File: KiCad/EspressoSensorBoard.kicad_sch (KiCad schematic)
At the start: 15 parts, among them IC1 FDC1004DGSR, J1 GRAPHIC DISPLAY IPS - 1.69", J2 MAX31855 (Temperature), J3 Screw_Terminal_01x02, J5 Pressure_Sensor, J7 Arduino_Nano_v3_Left, J8 Arduino_Nano_v3_Right, J9 Water_Level_Electrodes

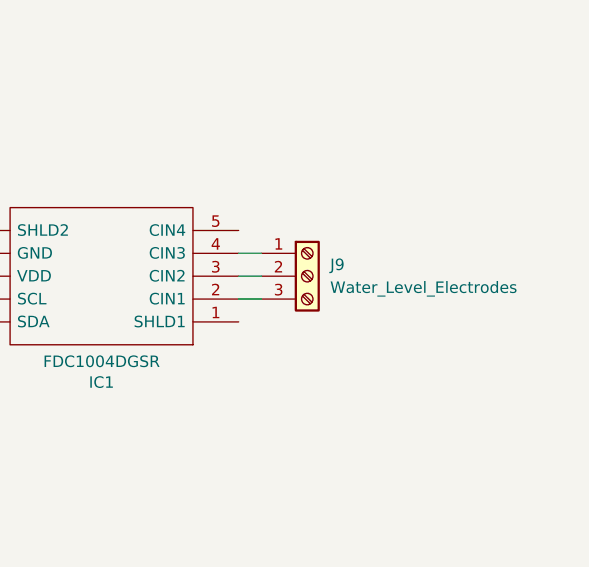
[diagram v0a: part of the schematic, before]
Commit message: Use SCHLD1 pin from the FDC1004 capacitive sensor
https://github.com/jcohenadad/espresso-pimpup/issues/43
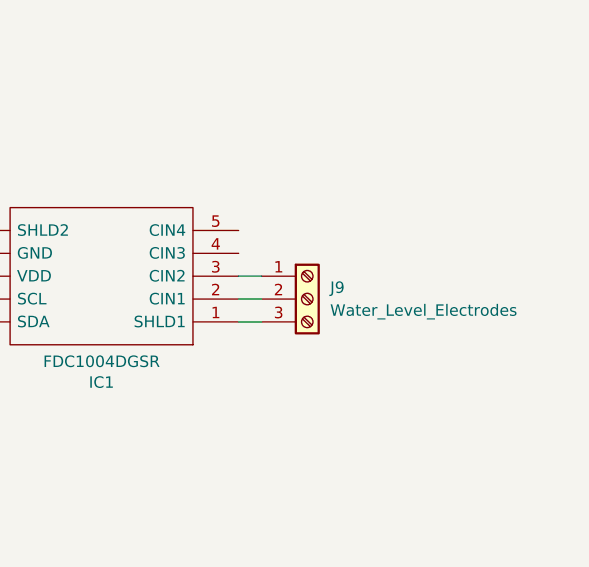
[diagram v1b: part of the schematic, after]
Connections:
- net at IC1.1 (SHLD1): now also J9.3 (Pin_3)
- net at IC1.2 (CIN1): now also J9.2 (Pin_2); no longer J9.3 (Pin_3)
- net at IC1.3 (CIN2): now also J9.1 (Pin_1); no longer J9.2 (Pin_2)
- net at IC1.4 (CIN3): no longer J9.1 (Pin_1)
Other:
- moved on the sheet: J9
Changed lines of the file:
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@@
+	(wire
+		(pts
+			(xy 222.25 58.42) (xy 224.79 58.42)
+		)
+		(stroke
+			(width 0)
+			(type default)
+		)
+	)
 	(wire
 		(pts
@@
 	(wire
 		(pts
-			(xy 222.25 58.42) (xy 224.79 58.42)
-		)
-		(stroke
-			(width 0)
-			(type default)
-		)
-	)
-	(wire
-		(pts
 			(xy 124.46 76.2) (xy 134.62 76.2)
 		)
@@
 	(wire
 		(pts
-			(xy 222.25 55.88) (xy 224.79 55.88)
-		)
-		(stroke
-			(width 0)
-			(type default)
-		)
-	)
-	(wire
-		(pts
 			(xy 130.81 63.5) (xy 134.62 63.5)
 		)
@@
 		(pts
 			(xy 222.25 60.96) (xy 224.79 60.96)
+		)
+		(stroke
+			(width 0)
+			(type default)
+		)
+	)
+	(wire
+		(pts
+			(xy 222.25 63.5) (xy 224.79 63.5)
 		)
 		(stroke
@@
 	(symbol
 		(lib_id "Connector:Screw_Terminal_01x03")
-		(at 229.87 58.42 0)
+		(at 229.87 60.96 0)
 		(unit 1)
 		(exclude_from_sim no)
@@
 		(fields_autoplaced yes)
 		(property "Reference" "J9"
-			(at 232.41 57.1499 0)
+			(at 232.41 59.6899 0)
 			(effects
 				(font
@@
 		)
 		(property "Value" "Water_Level_Electrodes"
-			(at 232.41 59.6899 0)
+			(at 232.41 62.2299 0)
 			(effects
 				(font
@@
 		)
 		(property "Footprint" "Connector_PinHeader_2.54mm:PinHeader_1x03_P2.54mm_Vertical"
-			(at 229.87 58.42 0)
+			(at 229.87 60.96 0)
 			(effects
 				(font
@@
 		)
 		(property "Datasheet" "~"
-			(at 229.87 58.42 0)
+			(at 229.87 60.96 0)
 			(effects
 				(font
@@
 		)
 		(property "Description" "Generic screw terminal, single row, 01x03, script generated (kicad-library-utils/schlib/autogen/connector/)"
-			(at 229.87 58.42 0)
-			(effects
-				(font
+			(at 229.87 60.96 0)
+			(effects
+				(font

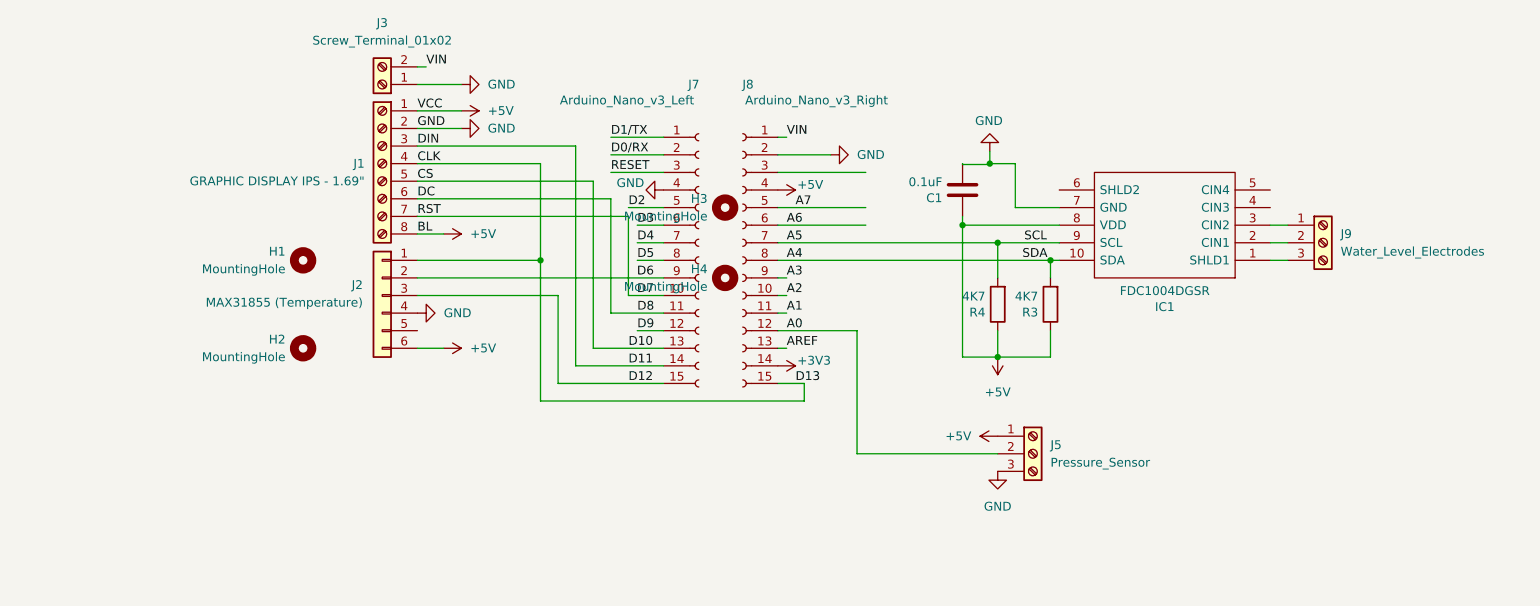
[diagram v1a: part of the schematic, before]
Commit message: Replaced screw terminal by Dupont male pins
https://github.com/jcohenadad/espresso-pimpup/issues/38
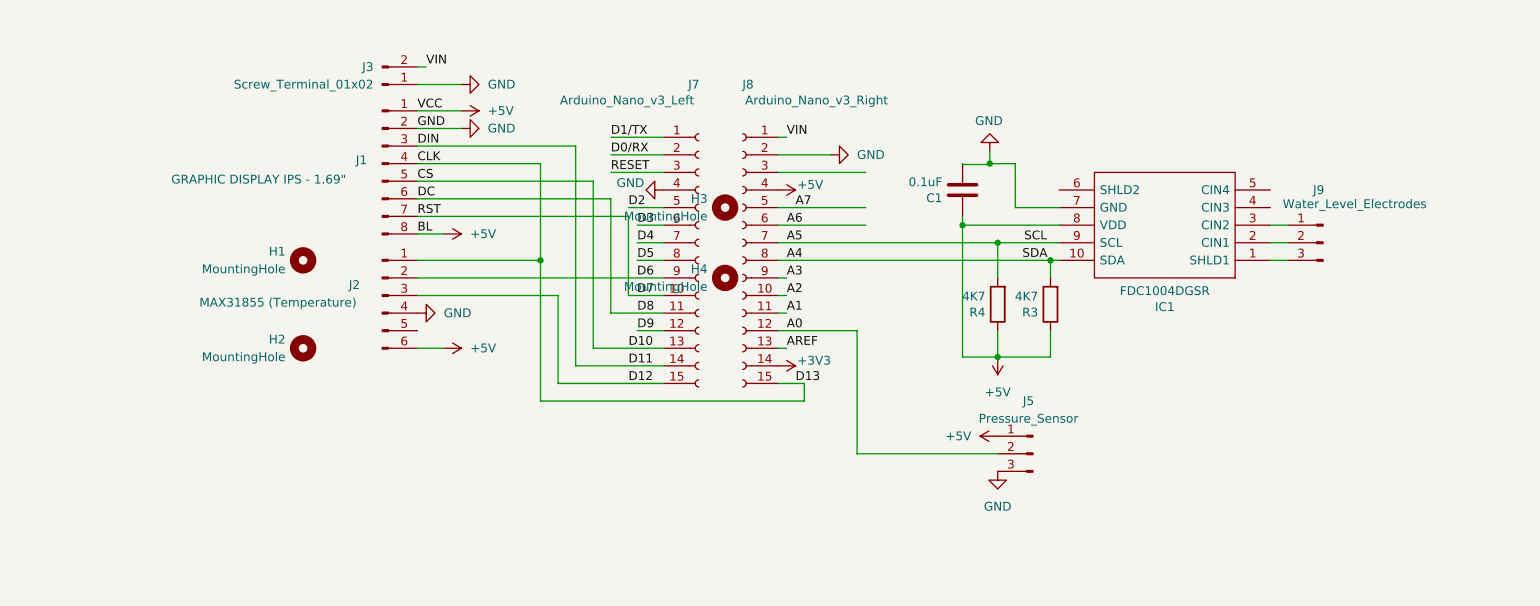
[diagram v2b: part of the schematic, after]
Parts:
- J1: symbol Connector:Screw_Terminal_01x08 -> Connector:Conn_01x08_Pin
- J2: symbol Connector_Generic:Conn_01x06 -> Connector:Conn_01x06_Pin
- J3: symbol Connector:Screw_Terminal_01x02 -> Connector:Conn_01x02_Pin
- J5, J9: symbol Connector:Screw_Terminal_01x03 -> Connector:Conn_01x03_Pin
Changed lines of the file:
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@@
 	)
 	(symbol
-		(lib_id "Connector_Generic:Conn_01x06")
+		(lib_id "Connector:Conn_01x06_Pin")
 		(at 93.98 68.58 0)
-		(mirror y)
 		(unit 1)
 		(exclude_from_sim no)
@@
 		(dnp no)
 		(property "Reference" "J2"
-			(at 91.186 67.056 0)
+			(at 89.154 67.056 0)
 			(effects
 				(font
@@
 		)
 		(property "Value" "MAX31855 (Temperature)"
-			(at 91.186 69.596 0)
+			(at 67.564 69.596 0)
 			(effects
 				(font
@@
 			)
 		)
-		(property "Datasheet" "https://learn.adafruit.com/thermocouple/downloads"
+		(property "Datasheet" "~"
 			(at 93.98 68.58 0)
 			(effects
@@
 			)
 		)
-		(property "Description" "Generic connector, single row, 01x06, script generated (kicad-library-utils/schlib/autogen/connector/)"
+		(property "Description" "Generic connector, single row, 01x06, script generated"
 			(at 93.98 68.58 0)
 			(effects
@@
 	)
 	(symbol
-		(lib_id "Connector:Screw_Terminal_01x03")
+		(lib_id "Connector:Conn_01x03_Pin")
 		(at 229.87 60.96 0)
-		(unit 1)
-		(exclude_from_sim no)
-		(in_bom yes)
-		(on_board yes)
-		(dnp no)
-		(fields_autoplaced yes)
+		(mirror y)
+		(unit 1)
+		(exclude_from_sim no)
+		(in_bom yes)
+		(on_board yes)
+		(dnp no)
 		(property "Reference" "J9"
-			(at 232.41 59.6899 0)
-			(effects
-				(font
-					(size 1.27 1.27)
-				)
-				(justify left)
+			(at 229.235 53.34 0)
+			(effects
+				(font
+					(size 1.27 1.27)
+				)
 			)
 		)
 		(property "Value" "Water_Level_Electrodes"
-			(at 232.41 62.2299 0)
-			(effects
-				(font
-					(size 1.27 1.27)
-				)
-				(justify left)
+			(at 234.442 55.372 0)
+			(effects
+				(font
+					(size 1.27 1.27)
+				)
 			)
 		)
@@
 			)
 		)
-		(property "Description" "Generic screw terminal, single row, 01x03, script generated (kicad-library-utils/schlib/autogen/connector/)"
+		(property "Description" "Generic connector, single row, 01x03, script generated"
 			(at 229.87 60.96 0)
 			(effects
@@
 	)
 	(symbol
-		(lib_id "Connector:Screw_Terminal_01x03")
+		(lib_id "Connector:Conn_01x03_Pin")
 		(at 187.96 91.44 0)
-		(unit 1)
-		(exclude_from_sim no)
-		(in_bom yes)
-		(on_board yes)
-		(dnp no)
-		(fields_autoplaced yes)
+		(mirror y)
+		(unit 1)
+		(exclude_from_sim no)
+		(in_bom yes)
+		(on_board yes)
+		(dnp no)
 		(property "Reference" "J5"
-			(at 190.5 90.1699 0)
-			(effects
-				(font
-					(size 1.27 1.27)
-				)
-				(justify left)
+			(at 187.325 83.82 0)
+			(effects
+				(font
+					(size 1.27 1.27)
+				)
 			)
 		)
 		(property "Value" "Pressure_Sensor"
-			(at 190.5 92.7099 0)
-			(effects
-				(font
-					(size 1.27 1.27)
-				)
-				(justify left)
+			(at 187.325 86.36 0)
+			(effects
+				(font
+					(size 1.27 1.27)
+				)
 			)
 		)
@@
 			)
 		)
-		(property "Description" "Generic screw terminal, single row, 01x03, script generated (kicad-library-utils/schlib/autogen/connector/)"
+		(property "Description" "Generic connector, single row, 01x03, script generated"
 			(at 187.96 91.44 0)
 			(effects
@@
 	)
 	(symbol
-		(lib_id "Connector:Screw_Terminal_01x02")
-		(at 93.98 38.1 180)
-		(unit 1)
-		(exclude_from_sim no)
-		(in_bom yes)
-		(on_board yes)
-		(dnp no)
-		(fields_autoplaced yes)
+		(lib_id "Connector:Conn_01x02_Pin")
+		(at 93.98 38.1 0)
+		(mirror x)
+		(unit 1)
+		(exclude_from_sim no)
+		(in_bom yes)
+		(on_board yes)
+		(dnp no)
 		(property "Reference" "J3"
-			(at 93.98 29.21 0)
-			(effects
-				(font
-					(size 1.27 1.27)
-				)
+			(at 92.71 35.5599 0)
+			(effects
+				(font
+					(size 1.27 1.27)
+				)
+				(justify right)
 			)
 		)
 		(property "Value" "Screw_Terminal_01x02"
-			(at 93.98 31.75 0)
-			(effects
-				(font
-					(size 1.27 1.27)
-				)
+			(at 92.71 38.0999 0)
+			(effects
+				(font
+					(size 1.27 1.27)
+				)
+				(justify right)
 			)
 		)
@@
 			)
 		)
-		(property "Description" "Generic screw terminal, single row, 01x02, script generated (kicad-library-utils/schlib/autogen/connector/)"
+		(property "Description" "Generic connector, single row, 01x02, script generated"
 			(at 93.98 38.1 0)
 			(effects
@@
 	)
 	(symbol
-		(lib_id "Connector:Screw_Terminal_01x08")
+		(lib_id "Connector:Conn_01x08_Pin")
 		(at 93.98 49.53 0)
-		(mirror y)
 		(unit 1)
 		(exclude_from_sim no)
@@
 		(dnp no)
 		(property "Reference" "J1"
-			(at 91.44 49.5299 0)
+			(at 90.17 49.022 0)
 			(effects
 				(font
@@
 		)
 		(property "Value" "GRAPHIC DISPLAY IPS - 1.69\""
-			(at 91.44 52.0699 0)
+			(at 63.5 51.816 0)
 			(effects
 				(font
@@
 			)
 		)
-		(property "Description" "Generic screw terminal, single row, 01x08, script generated (kicad-library-utils/schlib/autogen/connector/)"
+		(property "Description" "Generic connector, single row, 01x08, script generated"
 			(at 93.98 49.53 0)
 			(effects

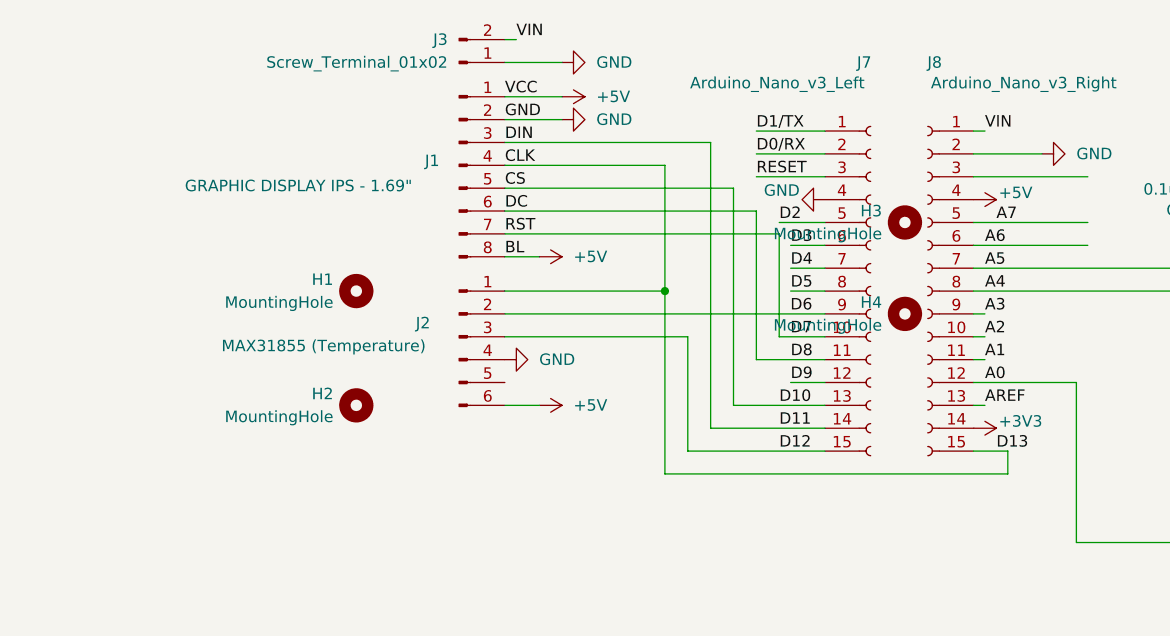
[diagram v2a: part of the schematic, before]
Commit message: Updated PCB and Arduino code
- Swapped D7 with D9 for easier routing
- Removed connection to RST on the Display (should work without it)
- Replaced connectors, notably using JST GH1.25mm for the display. https://github.com/jcohenadad/espresso-pimpup/issues/28
- Changed 3D model for Arduino. https://github.com/jcohenadad/espresso-pimpup/issues/44
- Connected pin to shielding on FDC1004. https://github.com/jcohenadad/espresso-pimpup/issues/41
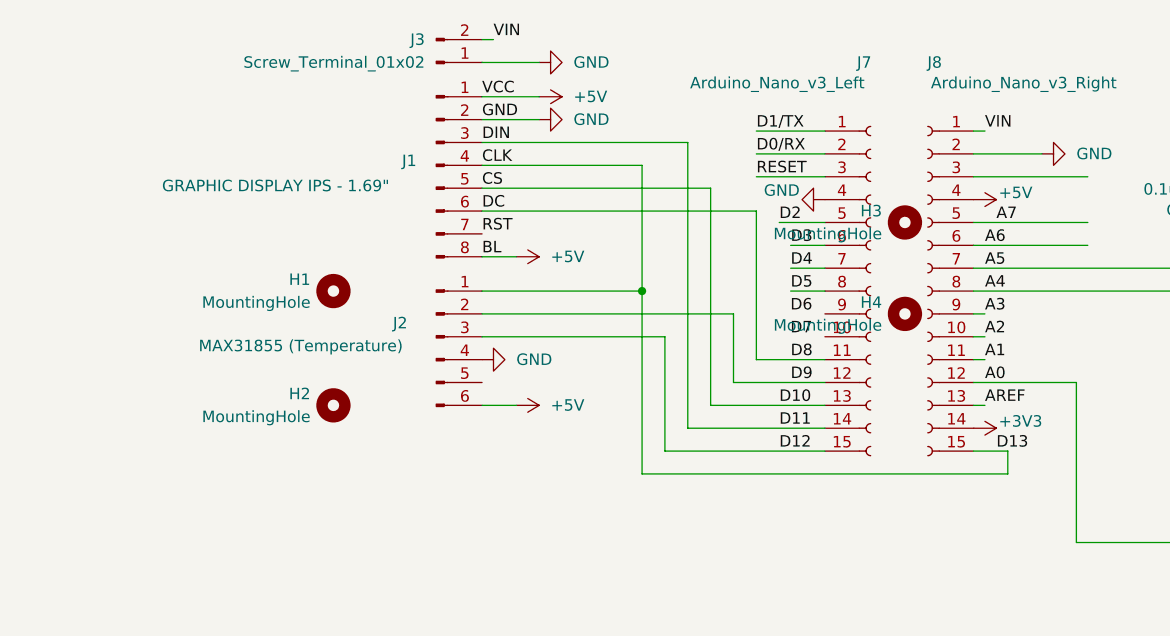
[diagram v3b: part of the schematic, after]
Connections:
- net D6: no longer J2.2 (Pin_2), J7.9 (Pin_9)
- net D7: no longer J1.7 (Pin_7), J7.10 (Pin_10)
- net D9: now also J2.2 (Pin_2)
- new net RST: J1.7 (Pin_7)
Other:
- moved on the sheet: H1, H2, J1, J2, J3

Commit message: Minor modifs on the Kicad PCD
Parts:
- J1: footprint Connector_PinHeader_2.54mm:PinHeader_1x08_P2.54mm_Vertical -> Connector_JST:JST_GH_BM08B-GHS-TBT_1x08-1MP_P1.25mm_Vertical
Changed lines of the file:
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@@
 			)
 		)
-		(property "Footprint" "Connector_PinHeader_2.54mm:PinHeader_1x08_P2.54mm_Vertical"
+		(property "Footprint" "Connector_JST:JST_GH_BM08B-GHS-TBT_1x08-1MP_P1.25mm_Vertical"
 			(at 91.44 49.53 0)
 			(effects

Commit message: Fixed arduino connector
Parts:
- J7, J8: footprint Connector_PinHeader_2.54mm:PinHeader_1x15_P2.54mm_Vertical -> Connector_PinSocket_2.54mm:PinSocket_1x15_P2.54mm_Vertical
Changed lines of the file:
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@@
 			)
 		)
-		(property "Footprint" "Connector_PinHeader_2.54mm:PinHeader_1x15_P2.54mm_Vertical"
+		(property "Footprint" "Connector_PinSocket_2.54mm:PinSocket_1x15_P2.54mm_Vertical"
 			(at 146.05 63.5 0)
 			(effects
@@
 			)
 		)
-		(property "Footprint" "Connector_PinHeader_2.54mm:PinHeader_1x15_P2.54mm_Vertical"
+		(property "Footprint" "Connector_PinSocket_2.54mm:PinSocket_1x15_P2.54mm_Vertical"
 			(at 139.7 63.5 0)
 			(effects
